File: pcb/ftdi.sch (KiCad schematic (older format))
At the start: 42 parts, among them U2 FT2232HL, U3 M93C46-WMN6TP, U4 MC74VHC1GT04DFT1, U5 74AHC125BQ,115, Y1 ECS-120-18-33-JEM-TR

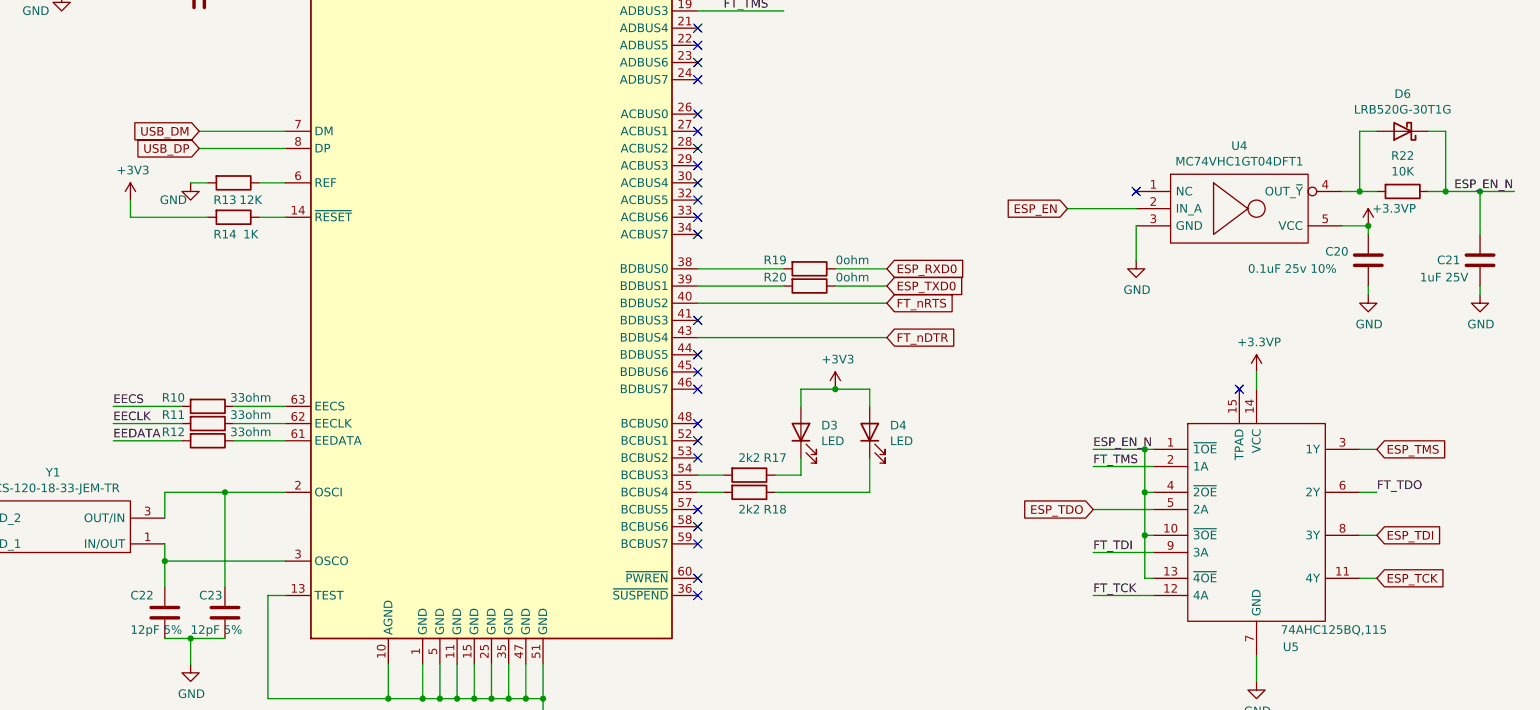
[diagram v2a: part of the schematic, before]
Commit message: - Se modifica el esquemático para respetar la estructura gerarquica
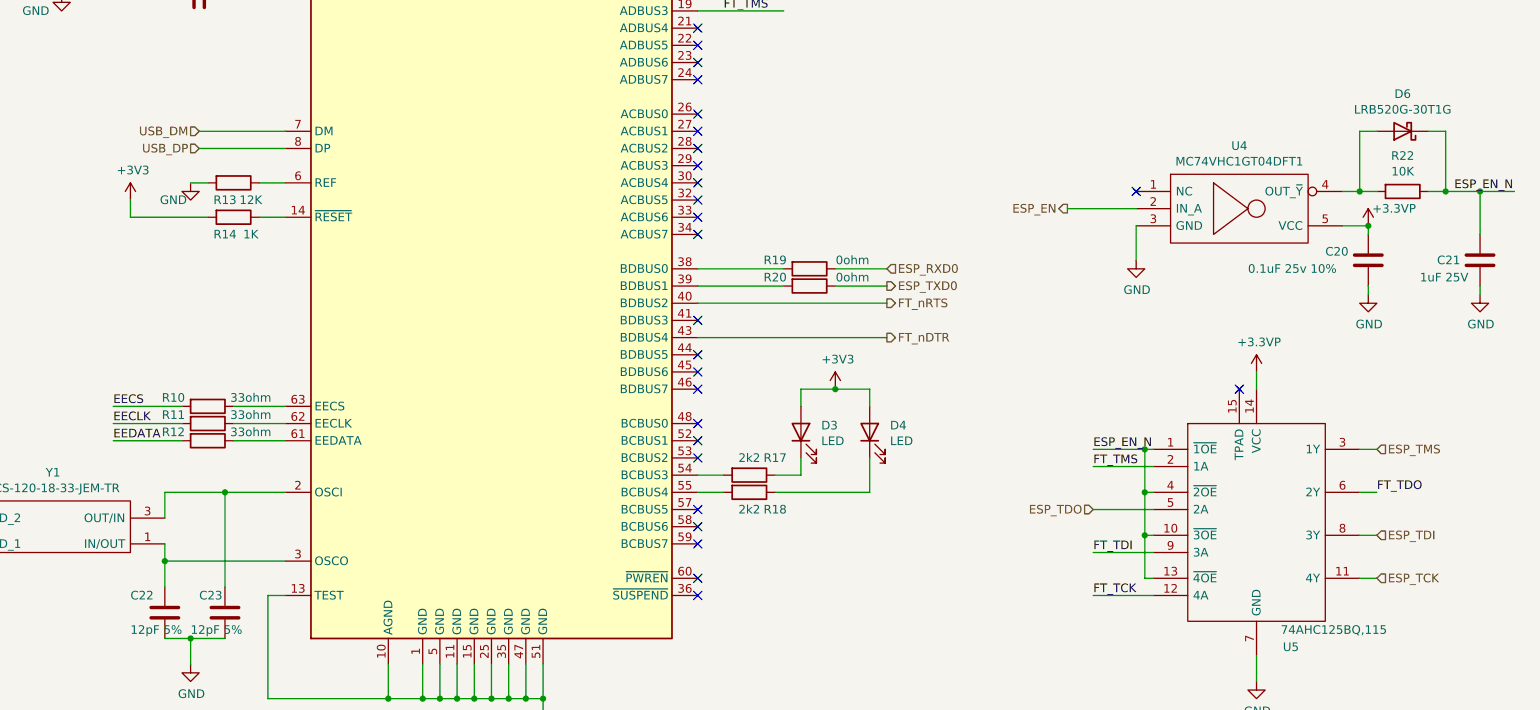
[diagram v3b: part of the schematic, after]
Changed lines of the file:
@@
 $Descr A4 11693 8268
 encoding utf-8
-Sheet 2 2
+Sheet 2 3
 Title "Espressif Programmer"
 Date ""
@@
 	4050 1350 4200 1350
 Connection ~ 4050 1350
-Text GLabel 8450 3200 0    50   Input ~ 0
-ESP_EN
-Text GLabel 7400 3650 2    50   Input ~ 0
-ESP_TXD0
-Text GLabel 7400 3550 2    50   Input ~ 0
-ESP_RXD0
-Text GLabel 7400 3950 2    50   Input ~ 0
-FT_nDTR
-Text GLabel 7400 3750 2    50   Input ~ 0
-FT_nRTS
 Text Label 6450 2050 0    50   ~ 0
 FT_TMS
@@
 Text Label 6450 1750 0    50   ~ 0
 FT_TCK
-Text GLabel 10250 4600 2    50   Input ~ 0
-ESP_TMS
-Text GLabel 10250 5100 2    50   Input ~ 0
-ESP_TDI
-Text GLabel 8600 4950 0    50   Input ~ 0
-ESP_TDO
-Text GLabel 10250 5350 2    50   Input ~ 0
-ESP_TCK
-Text GLabel 3400 2750 0    50   Input ~ 0
-USB_DM
-Text GLabel 3400 2850 0    50   Input ~ 0
-USB_DP
 Wire Wire Line
 	3550 750  3450 750
@@
 Wire Wire Line
 	10650 3100 10850 3100
+Text HLabel 3400 2750 0    50   Input ~ 0
+USB_DM
+Text HLabel 3400 2850 0    50   Input ~ 0
+USB_DP
+Text HLabel 8450 3200 0    50   Output ~ 0
+ESP_EN
+Text HLabel 7400 3550 2    50   Input ~ 0
+ESP_RXD0
+Text HLabel 7400 3650 2    50   Output ~ 0
+ESP_TXD0
+Text HLabel 7400 3750 2    50   Output ~ 0
+FT_nRTS
+Text HLabel 7400 3950 2    50   Output ~ 0
+FT_nDTR
+Text HLabel 8600 4950 0    50   Input ~ 0
+ESP_TDO
+Text HLabel 10250 4600 2    50   Input ~ 0
+ESP_TMS
+Text HLabel 10250 5100 2    50   Input ~ 0
+ESP_TDI
+Text HLabel 10250 5350 2    50   Input ~ 0
+ESP_TCK
 $EndSCHEMATC

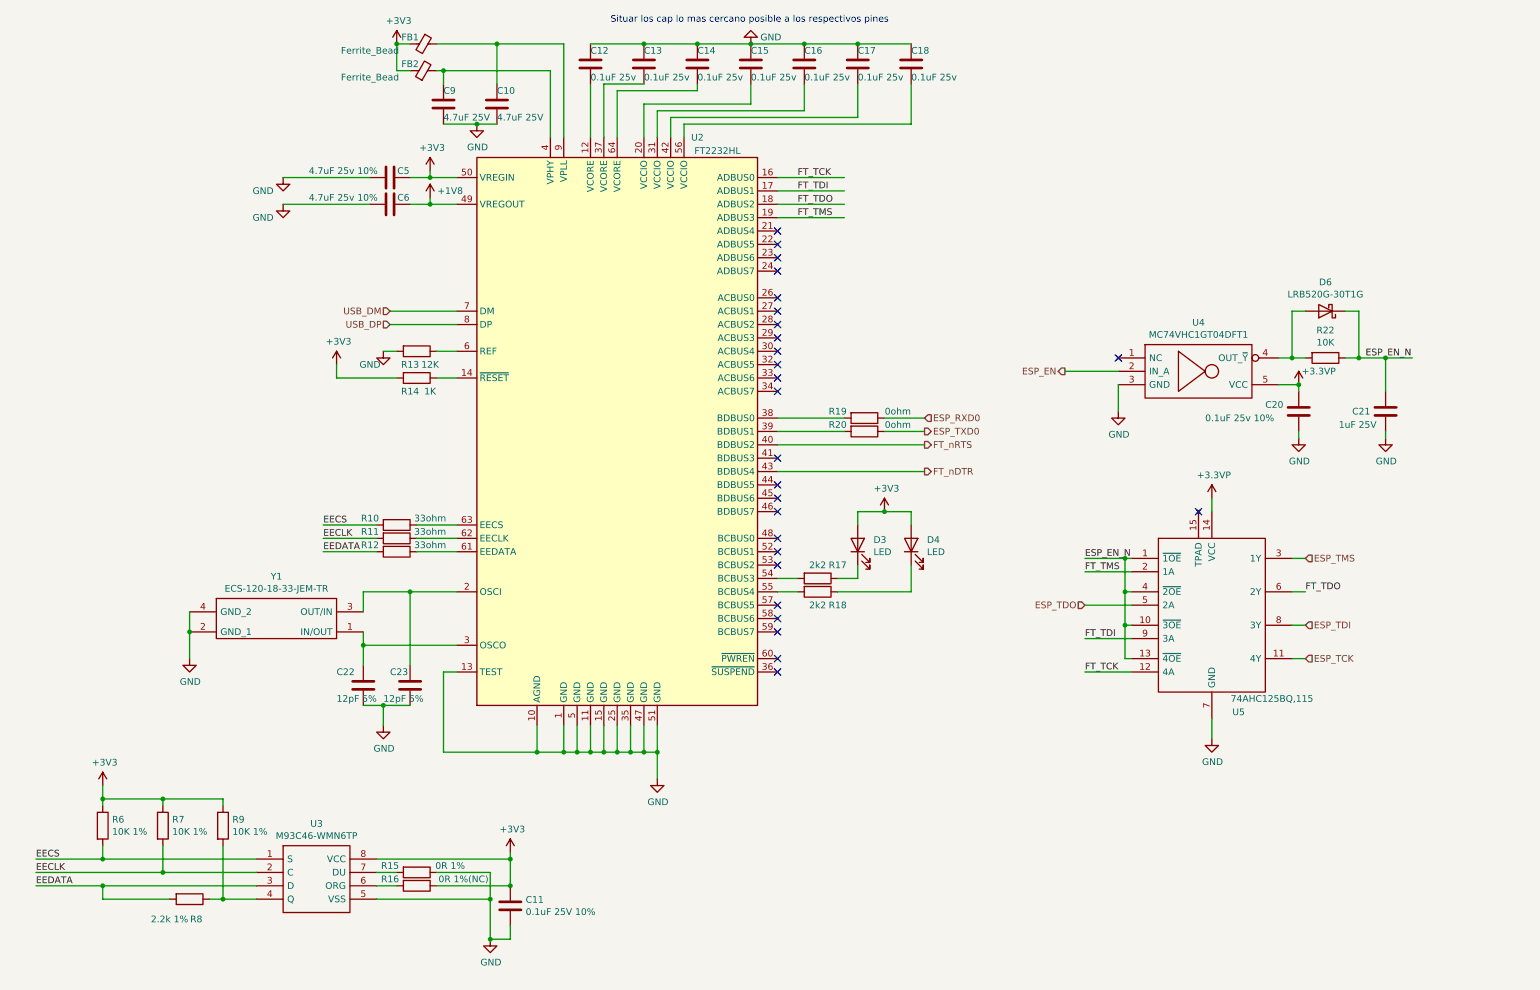
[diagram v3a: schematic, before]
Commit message: se agregan notas aclaratorias a los esquemáticos
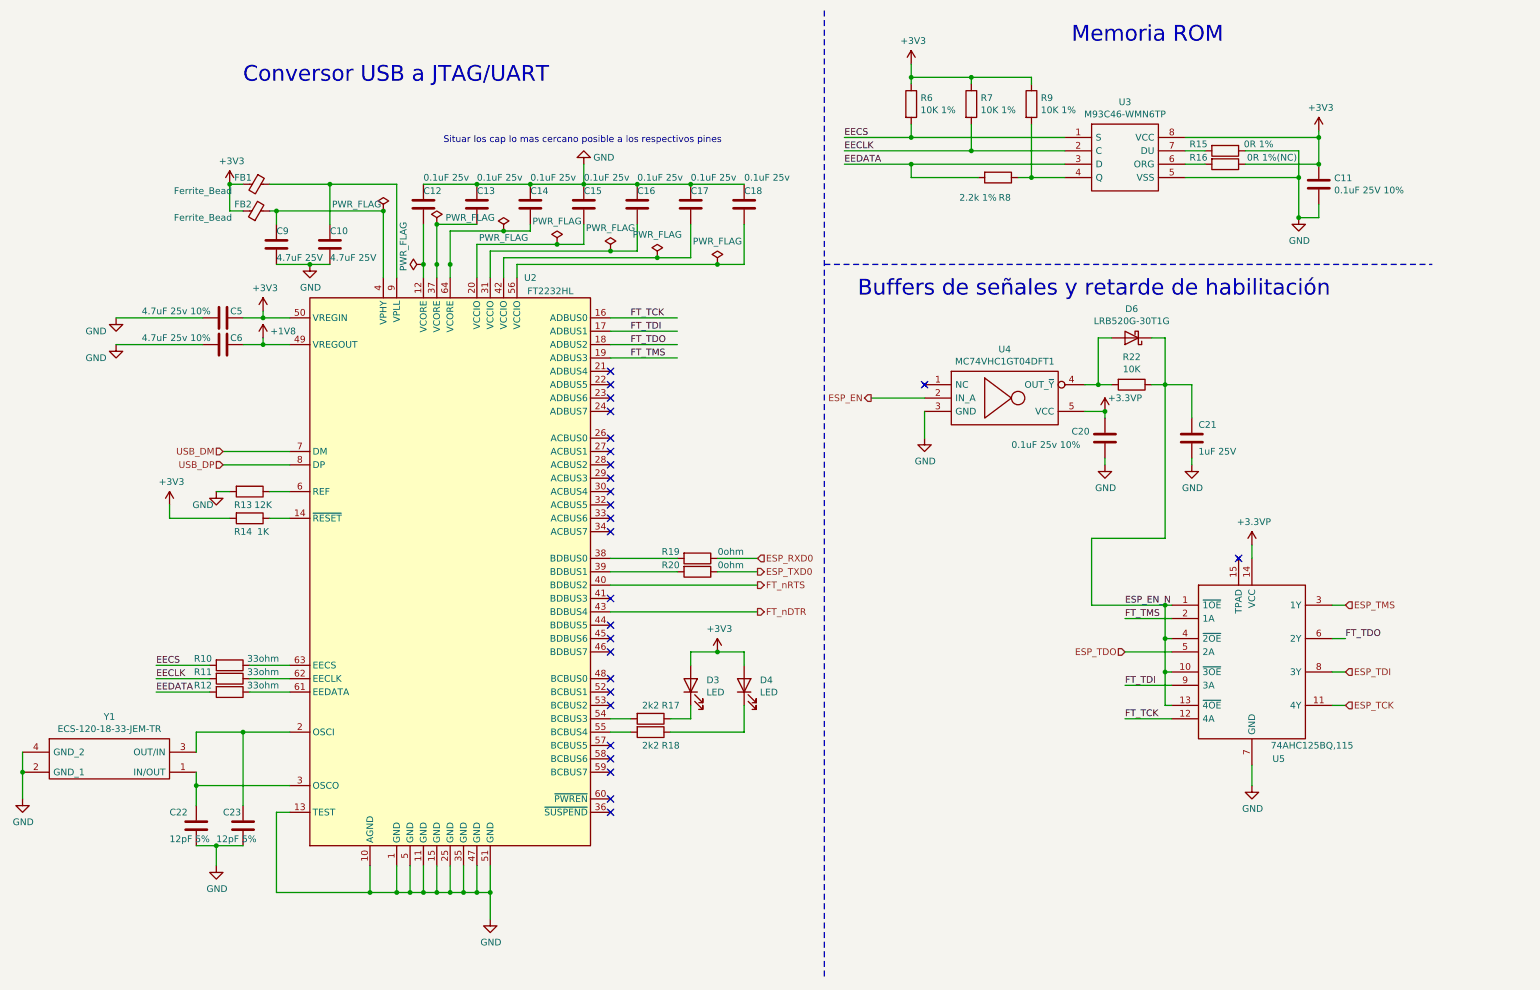
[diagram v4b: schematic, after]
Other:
- note added: "Buffers de señales y retarde de habilitación"
- note added: "Conversor USB a JTAG/UART"
- note added: "Memoria ROM"
- moved on the sheet: C10, C11, C12, C13, C14, C15, C16, C17, C18, C20, C21, C22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

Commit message: avances en el pcb y correcciones al esquematico
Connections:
- net +1V8: now also C12.2, C13.2, C14.2, U2.12 (VCORE), U2.37 (VCORE), U2.64 (VCORE)
- net +3V3: now also C15.2, C16.2, C17.2, C18.2, U2.20 (VCCIO), U2.31 (VCCIO), U2.42 (VCCIO), U2.56 (VCCIO)
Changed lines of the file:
@@
 	1    0    0    -1
 $EndComp
-Wire Wire Line
-	3650 2500 3650 2400
-Wire Wire Line
-	3750 2500 3750 2400
-Wire Wire Line
-	3750 2100 4050 2100
-Wire Wire Line
-	3850 2500 3850 2400
-Wire Wire Line
-	3850 2150 4250 2150
-Wire Wire Line
-	4450 2150 4450 2100
 $Comp
 L power:GND #PWR019
@@
 	1    0    0    -1
 $EndComp
-Wire Wire Line
-	4050 2500 4050 2250
-Wire Wire Line
-	4050 2250 4650 2250
-Wire Wire Line
-	4850 2250 4850 2100
-Wire Wire Line
-	4150 2500 4150 2300
-Wire Wire Line
-	4150 2300 5050 2300
-Wire Wire Line
-	5250 2300 5250 2100
-Wire Wire Line
-	4250 2500 4250 2350
-Wire Wire Line
-	4250 2350 5400 2350
-Wire Wire Line
-	5650 2350 5650 2100
-Wire Wire Line
-	4350 2500 4350 2400
-Wire Wire Line
-	4350 2400 5850 2400
-Wire Wire Line
-	6050 2400 6050 2100
 Connection ~ 4050 1800
-Connection ~ 4450 1800
 Wire Wire Line
 	4050 1800 4450 1800
 Connection ~ 4850 1800
-Wire Wire Line
-	4450 1800 4850 1800
 Connection ~ 5250 1800
 Wire Wire Line
@@
 Wire Wire Line
 	8650 4950 9200 4950
-$Comp
-L power:PWR_FLAG #FLG0101
-U 1 1 613E0B66
-P 3650 2400
-F 0 "#FLG0101" H 3650 2475 50  0001 C CNN
-F 1 "PWR_FLAG" H 3600 2550 50  0000 L CNN
-F 2 "" H 3650 2400 50  0001 C CNN
-F 3 "~" H 3650 2400 50  0001 C CNN
-	1    3650 2400
-	0    -1   -1   0
-$EndComp
-Connection ~ 3650 2400
-Wire Wire Line
-	3650 2400 3650 2100
-$Comp
-L power:PWR_FLAG #FLG0102
-U 1 1 613E2559
-P 3750 2100
-F 0 "#FLG0102" H 3750 2175 50  0001 C CNN
-F 1 "PWR_FLAG" H 4000 2150 50  0000 C CNN
-F 2 "" H 3750 2100 50  0001 C CNN
-F 3 "~" H 3750 2100 50  0001 C CNN
-	1    3750 2100
-	1    0    0    -1
-$EndComp
-Connection ~ 3750 2400
-Wire Wire Line
-	3750 2400 3750 2100
-$Comp
-L power:PWR_FLAG #FLG0103
-U 1 1 613E2EF3
-P 4250 2150
-F 0 "#FLG0103" H 4250 2225 50  0001 C CNN
-F 1 "PWR_FLAG" H 4250 2100 50  0000 C CNN
-F 2 "" H 4250 2150 50  0001 C CNN
-F 3 "~" H 4250 2150 50  0001 C CNN
-	1    4250 2150
-	1    0    0    -1
-$EndComp
-Connection ~ 3850 2400
-Wire Wire Line
-	3850 2400 3850 2150
-$Comp
-L power:PWR_FLAG #FLG0104
-U 1 1 613E3659
-P 5850 2400
-F 0 "#FLG0104" H 5850 2475 50  0001 C CNN
-F 1 "PWR_FLAG" H 5850 2573 50  0000 C CNN
-F 2 "" H 5850 2400 50  0001 C CNN
-F 3 "~" H 5850 2400 50  0001 C CNN
-	1    5850 2400
-	1    0    0    -1
-$EndComp
-Connection ~ 5850 2400
-Wire Wire Line
-	5850 2400 6050 2400
-$Comp
-L power:PWR_FLAG #FLG0105
-U 1 1 613E4889
-P 5400 2350
-F 0 "#FLG0105" H 5400 2425 50  0001 C CNN
-F 1 "PWR_FLAG" H 5400 2523 50  0000 C CNN
-F 2 "" H 5400 2350 50  0001 C CNN
-F 3 "~" H 5400 2350 50  0001 C CNN
-	1    5400 2350
-	1    0    0    -1
-$EndComp
-Connection ~ 5400 2350
-Wire Wire Line
-	5400 2350 5650 2350
-$Comp
-L power:PWR_FLAG #FLG0106
-U 1 1 613E4E6C
-P 5050 2300
-F 0 "#FLG0106" H 5050 2375 50  0001 C CNN
-F 1 "PWR_FLAG" H 5050 2473 50  0000 C CNN
-F 2 "" H 5050 2300 50  0001 C CNN
-F 3 "~" H 5050 2300 50  0001 C CNN
-	1    5050 2300
-	1    0    0    -1
-$EndComp
-Connection ~ 5050 2300
-Wire Wire Line
-	5050 2300 5250 2300
-$Comp
-L power:PWR_FLAG #FLG0107
-U 1 1 613E545A
-P 4650 2250
-F 0 "#FLG0107" H 4650 2325 50  0001 C CNN
-F 1 "PWR_FLAG" H 4650 2423 50  0000 C CNN
-F 2 "" H 4650 2250 50  0001 C CNN
-F 3 "~" H 4650 2250 50  0001 C CNN
-	1    4650 2250
-	1    0    0    -1
-$EndComp
-Connection ~ 4650 2250
-Wire Wire Line
-	4650 2250 4850 2250
 Wire Wire Line
 	4850 1800 4850 1650
-Connection ~ 4250 2150
-Wire Wire Line
-	4250 2150 4450 2150
-Connection ~ 3750 2100
 $Comp
 L power:PWR_FLAG #FLG0108
@@
 $EndComp
 Connection ~ 3350 2000
+Connection ~ 4450 1800
+Wire Wire Line
+	4450 1800 4850 1800
+Wire Wire Line
+	3650 2100 3650 2500
+Wire Wire Line
+	3850 2500 3750 2500
+Wire Wire Line
+	3750 2500 3650 2500
+Connection ~ 3750 2500
+Connection ~ 3650 2500
+Wire Wire Line
+	3650 2100 4050 2100
+Connection ~ 3650 2100
+Wire Wire Line
+	4450 2100 4050 2100
+Connection ~ 4050 2100
+$Comp
+L power:+1V8 #PWR0128
+U 1 1 612C0B16
+P 3850 2400
+F 0 "#PWR0128" H 3850 2250 50  0001 C CNN
+F 1 "+1V8" H 3865 2573 50  0000 C CNN
+F 2 "" H 3850 2400 50  0001 C CNN
+F 3 "" H 3850 2400 50  0001 C CNN
+	1    3850 2400
+	1    0    0    -1
+$EndComp
+Wire Wire Line
+	3850 2400 3850 2500
+Connection ~ 3850 2500
+Wire Wire Line
+	4050 2500 4150 2500
+Wire Wire Line
+	4150 2500 4250 2500
+Connection ~ 4150 2500
+Wire Wire Line
+	4250 2500 4350 2500
+Connection ~ 4250 2500
+Wire Wire Line
+	4350 2500 4850 2500
+Wire Wire Line
+	4850 2100 4850 2250
+Connection ~ 4350 2500
+Wire Wire Line
+	4850 2250 5250 2250
+Connection ~ 4850 2250
+Wire Wire Line
+	4850 2250 4850 2500
+Connection ~ 5250 2250
+Wire Wire Line
+	5250 2250 5250 2100
+Wire Wire Line
+	5250 2250 5650 2250
+Connection ~ 5650 2250
+Wire Wire Line
+	5650 2250 5650 2100
+Wire Wire Line
+	5650 2250 6050 2250
+Wire Wire Line
+	6050 2250 6050 2100
+$Comp
+L power:+3V3 #PWR0129
+U 1 1 6132FE79
+P 4250 2400
+F 0 "#PWR0129" H 4250 2250 50  0001 C CNN
+F 1 "+3V3" H 4265 2573 50  0000 C CNN
+F 2 "" H 4250 2400 50  0001 C CNN
+F 3 "" H 4250 2400 50  0001 C CNN
+	1    4250 2400
+	1    0    0    -1
+$EndComp
+Wire Wire Line
+	4250 2500 4250 2400
 $EndSCHEMATC
